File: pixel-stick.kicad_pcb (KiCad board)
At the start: 2 copper layers, 16.5 x 37.1 mm, 15 parts, among them J2 WS28**, U1 AZ1117-3.3, U2 ESP-01v090, U4 RT9361A, U5 74AHC1G125

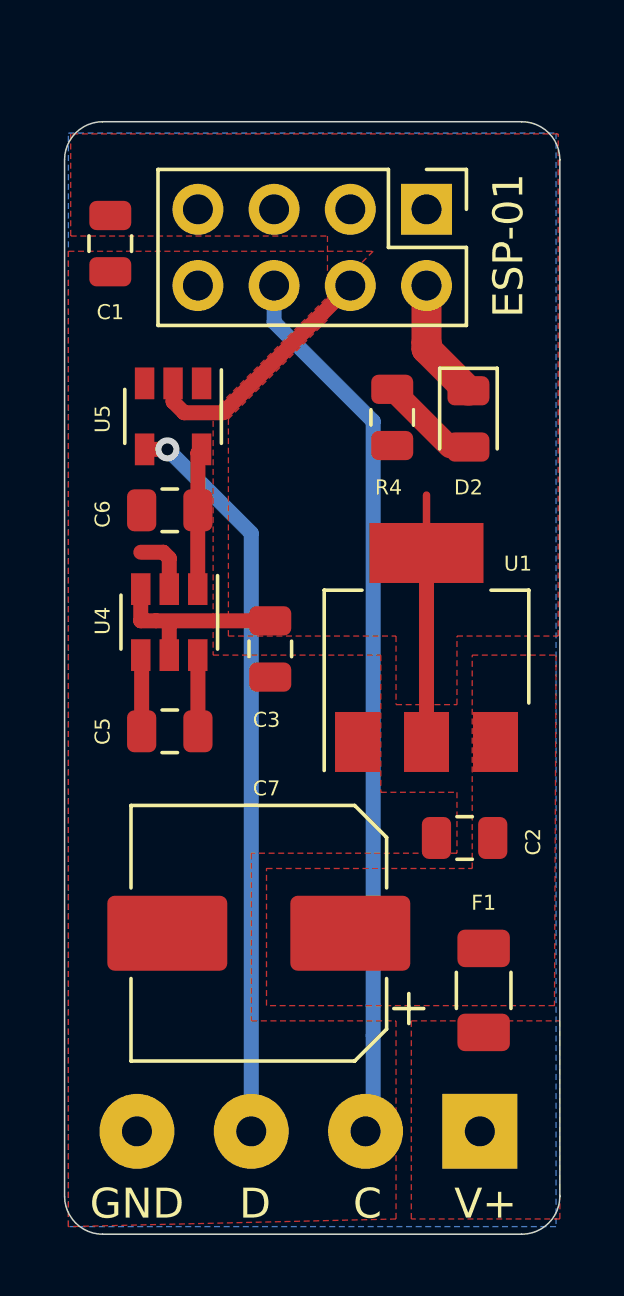
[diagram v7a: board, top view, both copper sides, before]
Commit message: increase passives to 1206 footprint
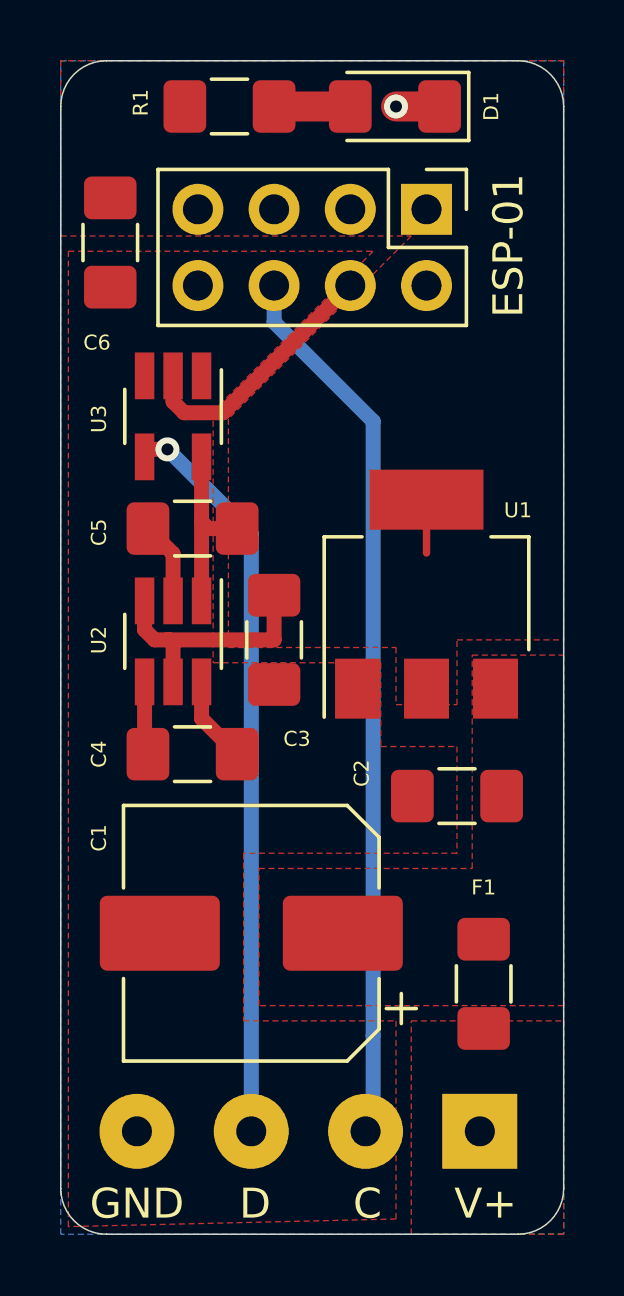
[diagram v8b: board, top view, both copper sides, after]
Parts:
- removed the C6 at (46.1, 66.5)
- removed C7: 100µF, Capacitor_SMD:CP_Elec_8x5.4
- removed D2: LED, LED_SMD:LED_0805_2012Metric
- removed R4: 120, Resistor_SMD:R_0805_2012Metric
- removed U4: RT9361A, Package_TO_SOT_SMD:SOT-23-6
- added C1: 100µF, Capacitor_SMD:CP_Elec_8x5.4, F.Cu at (48.8, 80.6)
- added C4: 1µF, Capacitor_SMD:C_1206_3216Metric_Pad1.42x1.75mm_HandSolder, F.Cu at (46.8, 74.7)
- added D1: LED, LED_SMD:LED_1206_3216Metric_Pad1.42x1.75mm_HandSolder, F.Cu at (53.6, 53.1)
- added R1: 120, Resistor_SMD:R_1206_3216Metric_Pad1.42x1.75mm_HandSolder, F.Cu at (48.0, 53.1)
- added U2: RT9361A, Package_TO_SOT_SMD:SOT-23-6_Handsoldering, F.Cu at (46.2, 70.9)
- C2, C3: footprint Capacitor_SMD:C_0805_2012Metric -> Capacitor_SMD:C_1206_3216Metric_Pad1.42x1.75mm_HandSolder
- C5: value 1µF -> 10µF; footprint Capacitor_SMD:C_0805_2012Metric -> Capacitor_SMD:C_1206_3216Metric_Pad1.42x1.75mm_HandSolder
- C6: renamed from C1; footprint Capacitor_SMD:C_0805_2012Metric -> Capacitor_SMD:C_1206_3216Metric_Pad1.42x1.75mm_HandSolder
- F1: footprint Resistor_SMD:R_1206_3216Metric -> Resistor_SMD:R_1206_3216Metric_Pad1.42x1.75mm_HandSolder
- U3: renamed from U5; footprint Package_TO_SOT_SMD:SOT-23-5 -> Package_TO_SOT_SMD:SOT-23-5_HandSoldering
- moved C5 6.80 mm to (46.8, 67.2)
- moved U1 1.78 mm to (54.6, 69.3)
- moved C2 1.42 mm to (55.6, 76.1)
- moved C3 0.33 mm to (49.5, 70.9)
- moved F1 0.22 mm to (56.5, 82.3)
- renumbered U2 to ESP-01, J2 to J1
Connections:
- net +VDC renamed Net-(C1-Pad1)
- C5 pad 1: Net-(C5-Pad1) -> +5V
- C5 pad 2: Net-(C5-Pad2) -> GND
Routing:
- net +3V3: track 14.7 -> 10.4 mm
- net Net-(D2-Pad2): track 3.34 -> 0.00 mm
- net Net-(C4-Pad1): track 0.00 -> 2.90 mm
- net Net-(C5-Pad2): track 2.55 -> 0.00 mm
- net Net-(C5-Pad1): track 2.54 -> 0.00 mm
- net Net-(D1-Pad2): track 0.00 -> 2.54 mm
- net Net-(C4-Pad2): track 0.00 -> 2.46 mm
- net GND: track 6.54 -> 4.39 mm, vias 0 -> 1
- net +5V: track 4.71 -> 6.08 mm
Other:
- board size 16.5 x 37.1 mm -> 16.8 x 39.1 mm
- board text added: "Board Version: 20191207a"
- board text removed: "Board Version: 20191206a"
